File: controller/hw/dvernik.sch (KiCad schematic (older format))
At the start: 30 parts, among them P101 WAGO233, P102 CONN_01X06, P103 CONN_01X02, U101 A25L40P, U102 EK-TM4C123GXL, U103 Itead_HC-05, U104 LP2992AIM5-3.3CT-ND

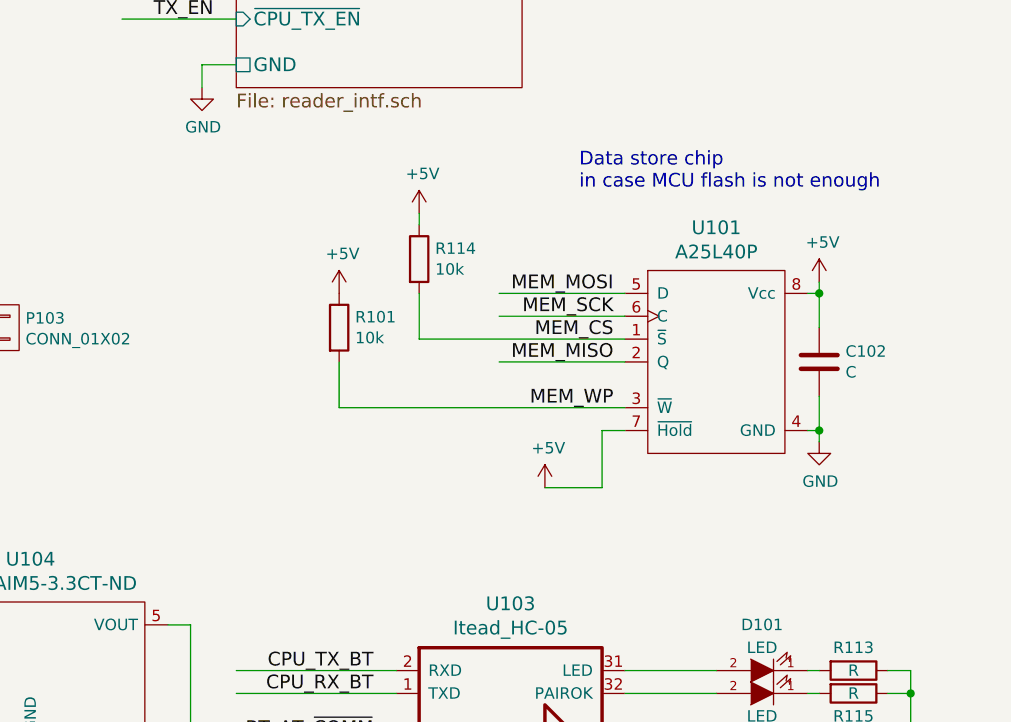
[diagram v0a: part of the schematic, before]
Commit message: Fix voltage for SPI flash, short under one capacitor
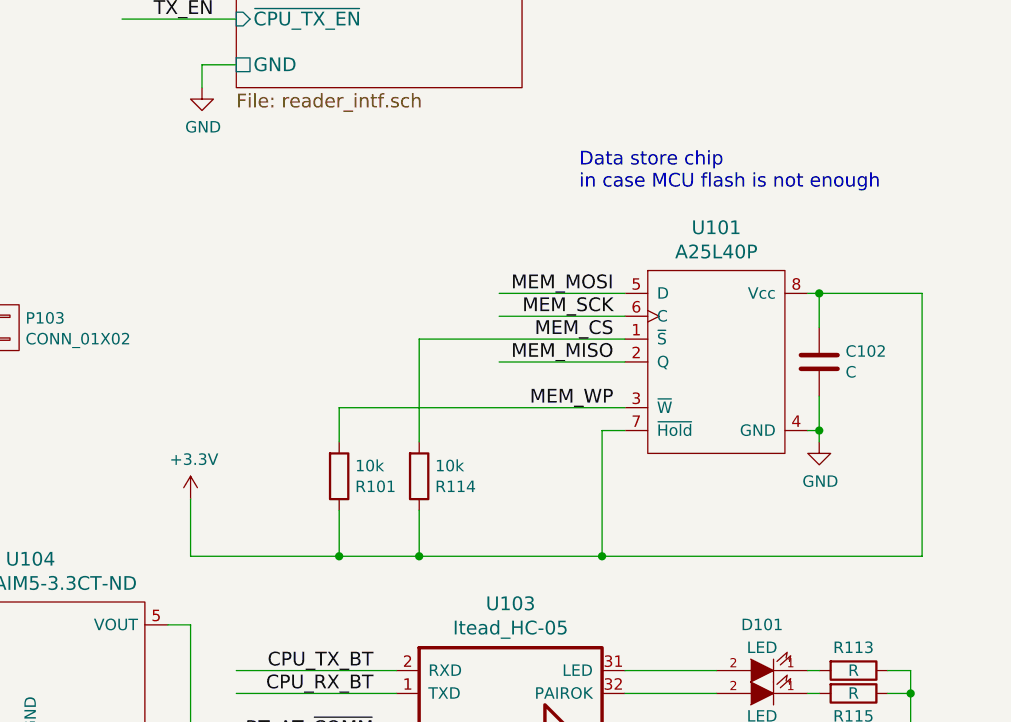
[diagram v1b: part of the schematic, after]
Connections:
- wire segments 138 -> 140
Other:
- moved on the sheet: R101, R114

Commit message: Compilability using embc lm4f, fixes to TX_EN switching
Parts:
- C101: symbol Jamicon_220uF_16V_TKP -> capacitors:Jamicon_220uF_16V_TKP
- C102, C103, C104, C105: symbol C -> simple:C
- D101, D102: symbol LED -> simple:LED
- P101: symbol CONN_01X03 -> connectors:CONN_01X03
- P102: symbol CONN_01X06 -> connectors:CONN_01X06
- P103: symbol CONN_01X02 -> connectors:CONN_01X02
- R101, R102, R103, R104, R105, R106, R107, R108, R109, R110, R111, R112, R113, R114, R115, R116: symbol R -> simple:R
- U101: symbol A25L40P -> ic:A25L40P
- U102: symbol EK-TM4C123GXL -> boards:EK-TM4C123GXL
- U103: symbol Itead_HC-05 -> rf:Itead_HC-05
- U104: symbol LP2992AIM5-3.3CT-ND -> power:LP2992AIM5-3.3CT-ND
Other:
- note added: "Configure ~TX_EN~ pin as Open Drain!\nIt has 5V pull-up and CPU\ncan only provide 3.3V"
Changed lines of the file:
@@
-EESchema Schematic File Version 2
-LIBS:74xx
-LIBS:boards
-LIBS:buttons
-LIBS:capacitors
-LIBS:connectors
-LIBS:cpu
-LIBS:discrete
-LIBS:drivers
-LIBS:ic
-LIBS:mspower
-LIBS:opto
-LIBS:passives
-LIBS:power
-LIBS:relay
-LIBS:rf
-LIBS:simple
-LIBS:transistors
-LIBS:templates
+EESchema Schematic File Version 4
 LIBS:dvernik-cache
 EELAYER 26 0
@@
 $EndDescr
 $Comp
-L EK-TM4C123GXL U102
+L boards:EK-TM4C123GXL U102
 U 1 1 58D7800E
 P 2600 3600
@@
 BATT_SENSE
 $Comp
-L R R104
+L simple:R R104
 U 1 1 58D8A8BF
 P 4650 3400
@@
 $EndComp
 $Comp
-L R R103
+L simple:R R103
 U 1 1 58D8A929
 P 4650 3000
@@
 $EndComp
 $Comp
-L GND #PWR01
+L mspower:GND #PWR01
 U 1 1 58D8AAFB
 P 4650 3550
@@
 PA0, PA1 - RX, TX serial line
 $Comp
-L +5V #PWR02
+L mspower:+5V #PWR02
 U 1 1 58D8FA2F
 P 3800 4800
@@
 $EndComp
 $Comp
-L +3.3V #PWR03
+L mspower:+3.3V #PWR03
 U 1 1 58D8FC00
 P 1300 4800
@@
 MEM_WP
 $Comp
-L A25L40P U101
+L ic:A25L40P U101
 U 1 1 58D9C69A
 P 10150 3400
@@
 $EndComp
 $Comp
-L GND #PWR04
+L mspower:GND #PWR04
 U 1 1 58D9CED8
 P 10600 3750
@@
 MEM_WP
 $Comp
-L R R101
+L simple:R R101
 U 1 1 58D9D4B8
 P 8500 3900
@@
 $EndComp
 $Comp
-L R R114
+L simple:R R114
 U 1 1 58D9D87F
 P 8850 3900
@@
 $EndComp
 $Comp
-L C C102
+L simple:C C102
 U 1 1 58D9DEDA
 P 10600 3400
@@
 CPU_TX
 $Comp
-L +5V #PWR05
+L mspower:+5V #PWR05
 U 1 1 58E1B5F9
 P 7750 1050
@@
 $EndSheet
 $Comp
-L GND #PWR06
+L mspower:GND #PWR06
 U 1 1 58FEB1F0
 P 4250 7250
@@
 $EndComp
 $Comp
-L +5V #PWR07
+L mspower:+5V #PWR07
 U 1 1 58FEBB8D
 P 2350 5800
@@
 $EndComp
 $Comp
-L GND #PWR08
+L mspower:GND #PWR08
 U 1 1 58FEBE71
 P 2350 7100
@@
 Standard buzzer needs\nabout 12V 600mA
 $Comp
-L +12V #PWR09
+L mspower:+12V #PWR09
 U 1 1 590DB5FC
 P 4250 5850
@@
 $EndComp
 $Comp
-L Jamicon_220uF_16V_TKP C101
+L capacitors:Jamicon_220uF_16V_TKP C101
 U 1 1 590DEE5A
 P 4800 7000
@@
 $EndComp
 $Comp
-L GND #PWR010
+L mspower:GND #PWR010
 U 1 1 590E4616
 P 3600 1600
@@
 $EndComp
 $Comp
-L +12V #PWR011
+L mspower:+12V #PWR011
 U 1 1 590E486A
 P 3450 800
@@
 $EndComp
 $Comp
-L +5V #PWR012
+L mspower:+5V #PWR012
 U 1 1 590E4F6C
 P 3250 800
@@
 $EndComp
 $Comp
-L CONN_01X03 P101
+L connectors:CONN_01X03 P101
 U 1 1 590EC2E4
 P 7100 6000
@@
 $EndComp
 $Comp
-L +5V #PWR013
+L mspower:+5V #PWR013
 U 1 1 590EC4CC
 P 6650 5550
@@
 $EndComp
 $Comp
-L GND #PWR014
+L mspower:GND #PWR014
 U 1 1 590EC5E4
 P 6650 6150
@@
 DCF77
 $Comp
-L R R102
+L simple:R R102
 U 1 1 590ECD1C
 P 6250 5800
@@
 BUZZ1
 $Comp
-L R R105
+L simple:R R105
 U 1 1 59171858
 P 2050 5850
@@
 $EndSheet
 $Comp
-L GND #PWR015
+L mspower:GND #PWR015
 U 1 1 5917B7B2
 P 7900 2200
@@
 ~READER_ON
 $Comp
-L R R106
+L simple:R R106
 U 1 1 5918956C
 P 5700 6000
@@
 	4300 3500 4300 4850
 $Comp
-L R R108
+L simple:R R108
 U 1 1 59194260
 P 5250 5050
@@
 $EndComp
 $Comp
-L R R107
+L simple:R R107
 U 1 1 59194267
 P 5250 4650
@@
 $EndComp
 $Comp
-L GND #PWR016
+L mspower:GND #PWR016
 U 1 1 5919426E
 P 5650 4500
@@
 Connection ~ 5650 4150
 $Comp
-L R R110
+L simple:R R110
 U 1 1 5919451F
 P 5650 4350
@@
 $EndComp
 $Comp
-L R R109
+L simple:R R109
 U 1 1 59194526
 P 5650 3950
@@
 $EndComp
 $Comp
-L GND #PWR017
+L mspower:GND #PWR017
 U 1 1 5919452D
 P 5250 5200
@@
 CHARGE_SENSE2
 $Comp
-L +BATT #PWR018
+L mspower:+BATT #PWR018
 U 1 1 59195961
 P 4650 2850
@@
 	5650 3800 4900 3800
 $Comp
-L +BATT #PWR019
+L mspower:+BATT #PWR019
 U 1 1 5917AB39
 P 5550 1050
@@
 	5150 1100 5000 1100
 $Comp
-L CONN_01X06 P102
+L connectors:CONN_01X06 P102
 U 1 1 5917AD72
 P 4800 1350
@@
 $EndComp
 $Comp
-L GND #PWR020
+L mspower:GND #PWR020
 U 1 1 5917AEBF
 P 5150 1650
@@
 	5550 1200 5550 1050
 $Comp
-L VCC #PWR021
+L mspower:VCC #PWR021
 U 1 1 5917C330
 P 6150 1350
@@
 $EndComp
 $Comp
-L R R112
+L simple:R R112
 U 1 1 5917D128
 P 800 3800
@@
 $EndComp
 $Comp
-L R R111
+L simple:R R111
 U 1 1 5917D12E
 P 800 3400
@@
 $EndComp
 $Comp
-L GND #PWR022
+L mspower:GND #PWR022
 U 1 1 5917D134
 P 800 3950
@@
 Connection ~ 800  3600
 $Comp
-L VCC #PWR023
+L mspower:VCC #PWR023
 U 1 1 5917D381
 P 800 3250
@@
 $EndComp
 $Comp
-L Itead_HC-05 U103
+L rf:Itead_HC-05 U103
 U 1 1 59185F5C
 P 9250 5050
@@
 	7850 5350 8750 5350
 $Comp
-L GND #PWR024
+L mspower:GND #PWR024
 U 1 1 59186D47
 P 8650 5500
@@
 $EndComp
 $Comp
-L GND #PWR025
+L mspower:GND #PWR025
 U 1 1 59186DE1
 P 9900 5500
@@
 	8650 5450 8650 5500
 $Comp
-L C C103
+L simple:C C103
 U 1 1 591870F8
 P 8300 5550
@@
 $EndComp
 $Comp
-L GND #PWR026
+L mspower:GND #PWR026
 U 1 1 59187554
 P 8300 5700
@@
 Connection ~ 8300 5350
 $Comp
-L LED D101
+L simple:LED D101
 U 1 1 59187BB8
 P 10350 4750
@@
 $EndComp
 $Comp
-L LED D102
+L simple:LED D102
 U 1 1 59187D14
 P 10350 4850
@@
 $EndComp
 $Comp
-L R R113
+L simple:R R113
 U 1 1 591880F0
 P 10750 4750
@@
 $EndComp
 $Comp
-L R R115
+L simple:R R115
 U 1 1 591881EF
 P 10750 4850
@@
 	1700 4300 1100 4300
 $Comp
-L GND #PWR027
+L mspower:GND #PWR027
 U 1 1 59186DCC
 P 1600 4950
@@
 $EndComp
 $Comp
-L GND #PWR028
+L mspower:GND #PWR028
 U 1 1 59186E70
 P 3600 4950
@@
 	6150 1500 6150 1350
 $Comp
-L LP2992AIM5-3.3CT-ND U104
+L power:LP2992AIM5-3.3CT-ND U104
 U 1 1 59186A1A
 P 7150 4750
@@
 $EndComp
 $Comp
-L +5V #PWR029
+L mspower:+5V #PWR029
 U 1 1 59186B3D
 P 6400 4550
@@
 Connection ~ 6400 4550
 $Comp
-L C C105
+L simple:C C105
 U 1 1 59186E3C
 P 6350 5000
@@
 $EndComp
 $Comp
-L GND #PWR030
+L mspower:GND #PWR030
 U 1 1 59186F55
 P 7150 5250
@@
 $EndComp
 $Comp
-L C C104
+L simple:C C104
 U 1 1 5918705F
 P 6100 4700
@@
 TAMPER
 $Comp
-L CONN_01X02 P103
+L connectors:CONN_01X02 P103
 U 1 1 591885DC
 P 7050 3250
@@
 $EndComp
 $Comp
-L GND #PWR031
+L mspower:GND #PWR031
 U 1 1 5918871E
 P 6800 3400
@@
 TAMPER
 $Comp
-L R R116
+L simple:R R116
 U 1 1 59188BA4
 P 6350 3000
@@
 $EndComp
 $Comp
-L +5V #PWR032
+L mspower:+5V #PWR032
 U 1 1 59188CD6
 P 6350 2850
@@
 	7850 4250 7850 4000
 $Comp
-L +3.3V #PWR033
+L mspower:+3.3V #PWR033
 U 1 1 593C7D18
 P 7850 4000
@@
 Wire Wire Line
 	10600 3250 10600 3100
+Text Notes 650  5600 0    60   ~ 0
+Configure ~TX_EN~ pin as Open Drain!\nIt has 5V pull-up and CPU\ncan only provide 3.3V
+Wire Notes Line
+	1000 5300 1000 3700
+Wire Notes Line
+	1000 3700 1050 3700
 $EndSCHEMATC

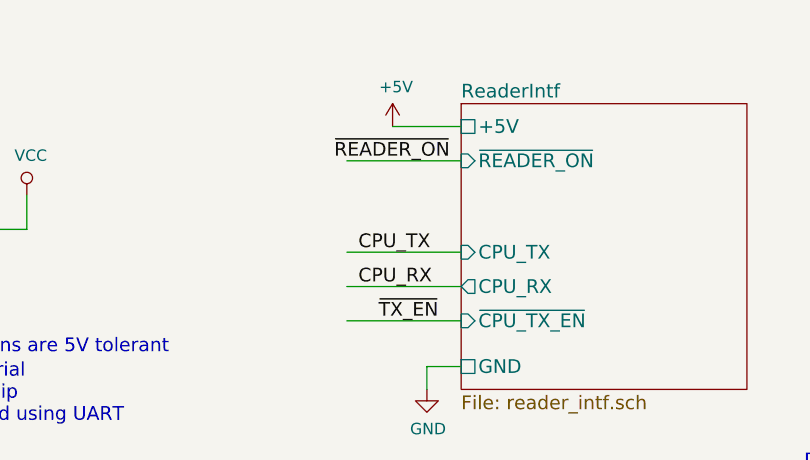
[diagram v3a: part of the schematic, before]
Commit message: Fix serious hw bug (5V level on 3.3V tolerant RX/TX on ctrl board)
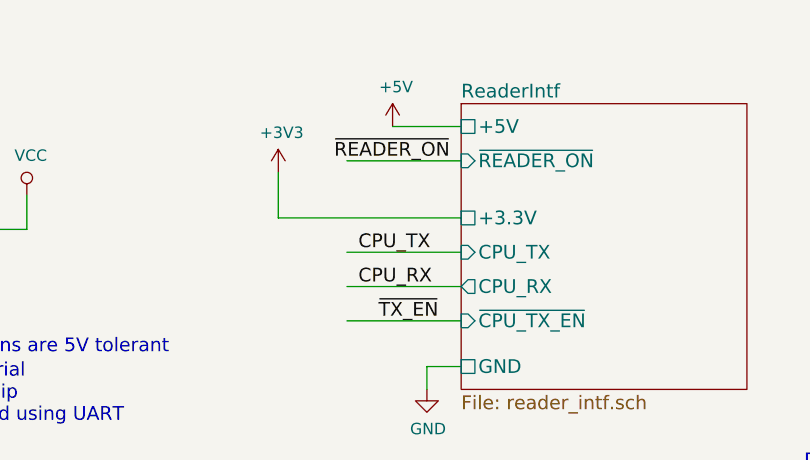
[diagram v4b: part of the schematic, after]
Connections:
- net labels added: +3V3
- wire segments 140 -> 142
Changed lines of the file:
@@
 Sheet 1 4
 Title ""
-Date ""
-Rev ""
+Date "2017-11-28"
+Rev "1.2"
 Comp ""
 Comment1 ""
@@
 F6 "+5V" U L 8050 1050 60
 F7 "~READER_ON" I L 8050 1200 60
+F8 "+3.3V" U L 8050 1450 60
 $EndSheet
 $Comp
@@
 Wire Notes Line
 	1000 3700 1050 3700
+Wire Wire Line
+	8050 1450 7250 1450
+Wire Wire Line
+	7250 1450 7250 1250
+$Comp
+L mspower:+3V3 #PWR044
+U 1 1 5A2C4F8D
+P 7250 1250
+F 0 "#PWR044" H 7250 1100 50  0001 C CNN
+F 1 "+3V3" H 7265 1423 50  0000 C CNN
+F 2 "" H 7250 1250 60  0000 C CNN
+F 3 "" H 7250 1250 60  0000 C CNN
+	1    7250 1250
+	1    0    0    -1
+$EndComp
 $EndSCHEMATC

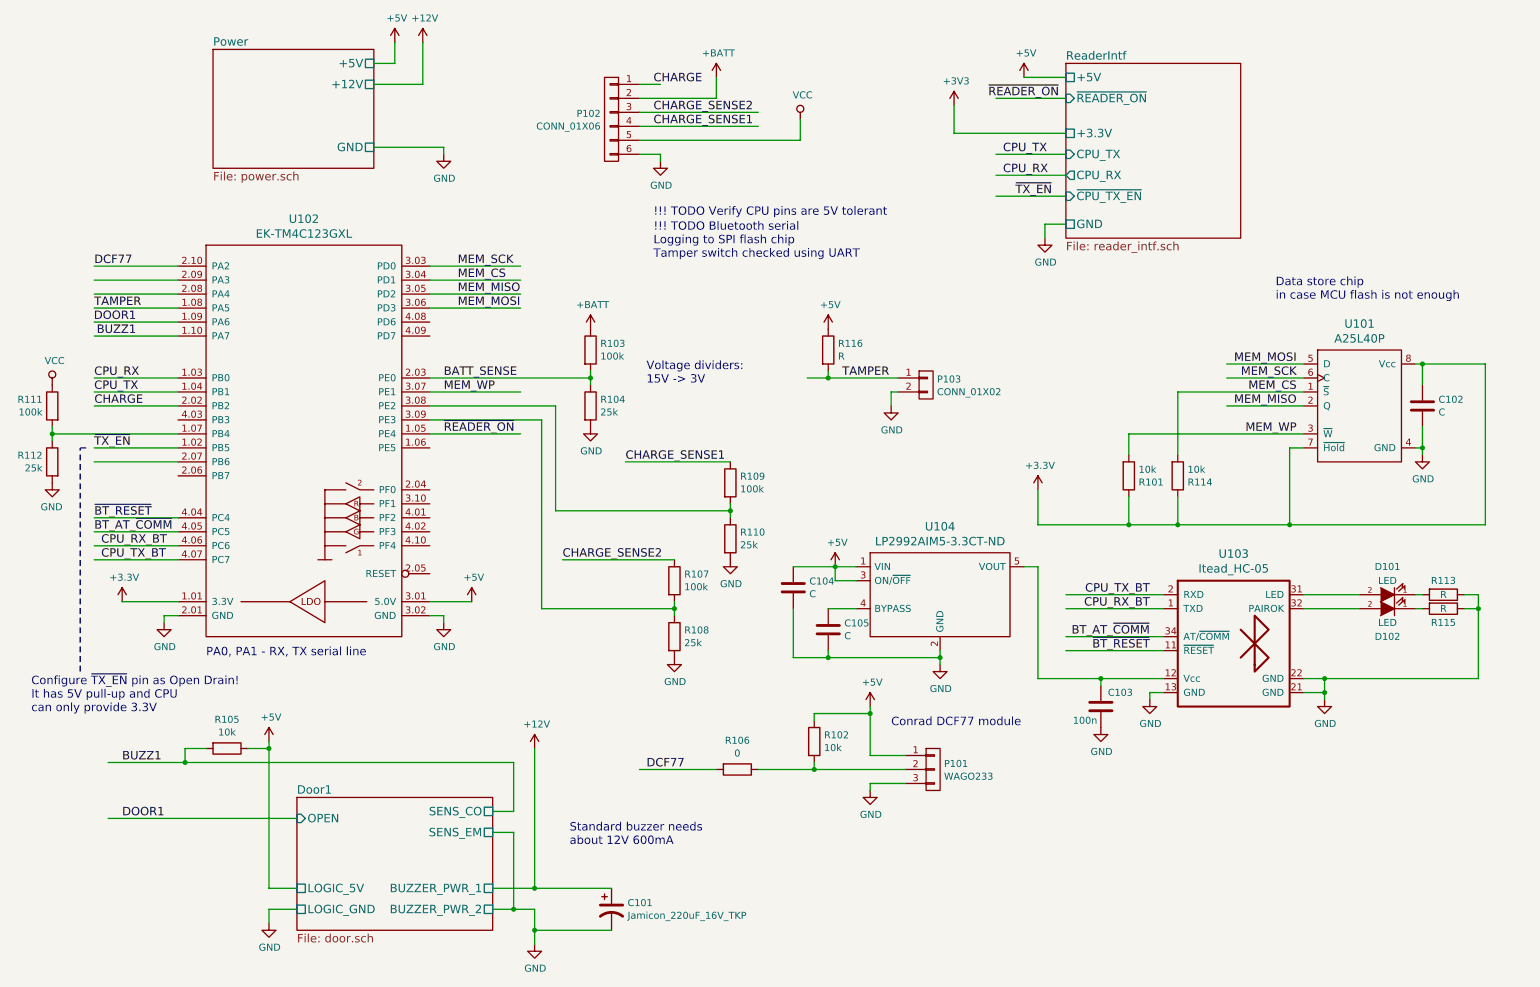
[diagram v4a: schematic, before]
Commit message: WIP Still working in 3.3 - 5V interface issues
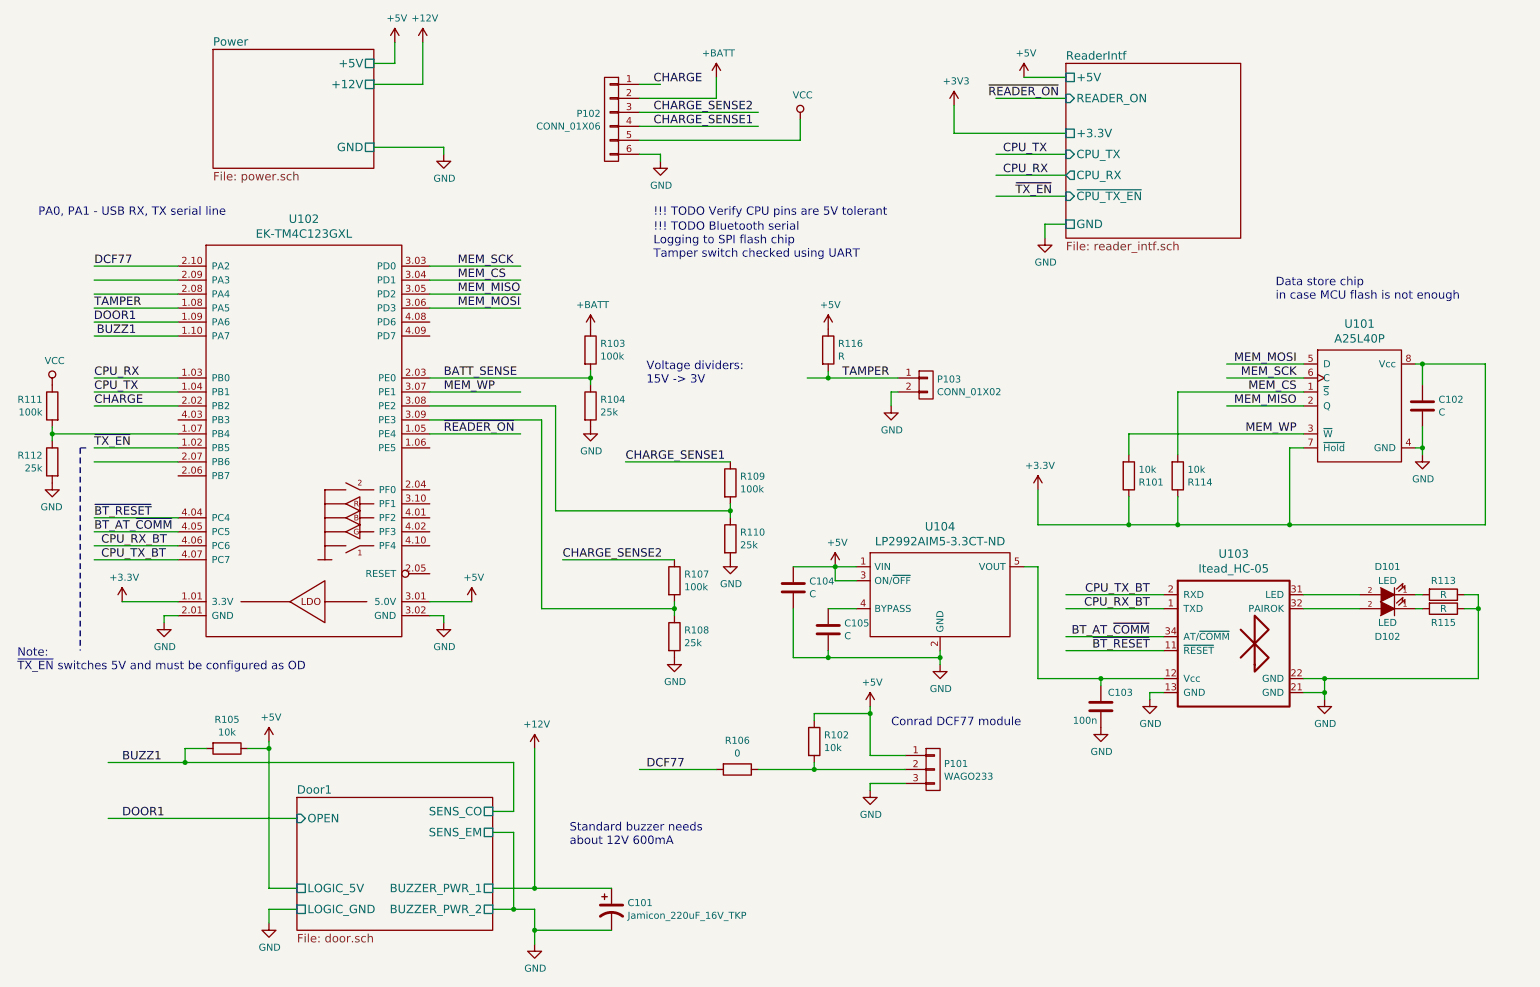
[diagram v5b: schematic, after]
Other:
- note added: "Note:\n~TX_EN~ switches 5V and must be configured as OD\n"
- note added: "PA0, PA1 - USB RX, TX serial line"
- note removed: "Configure ~TX_EN~ pin as Open Drain!\nIt has 5V pull-up and CPU\ncan only provide 3.3V"
- note removed: "PA0, PA1 - RX, TX serial line"
